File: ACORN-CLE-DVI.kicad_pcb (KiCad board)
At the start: 4 copper layers, 2 parts, among them J1 HDMI_A, U1 PI3HDX511D

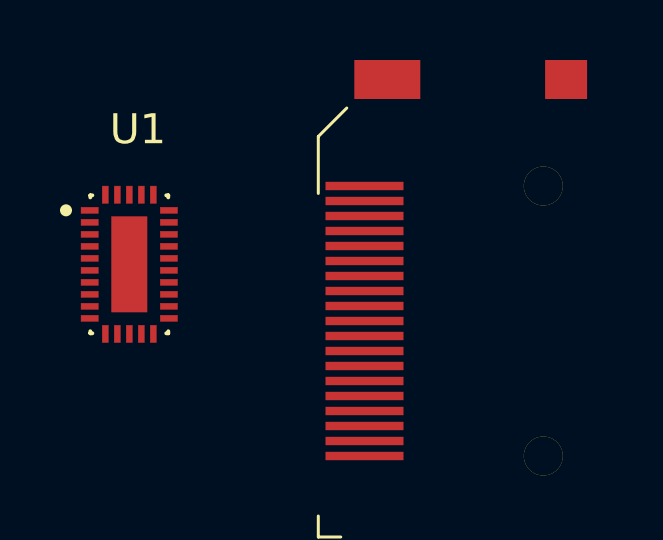
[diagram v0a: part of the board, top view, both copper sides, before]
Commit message: routed differential pairs
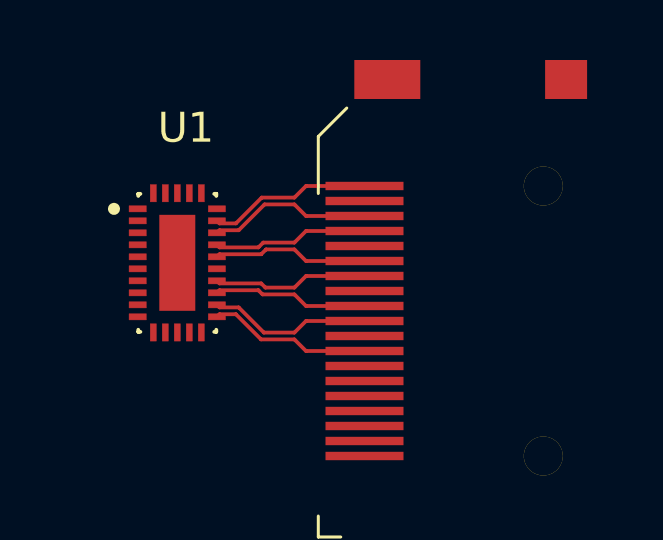
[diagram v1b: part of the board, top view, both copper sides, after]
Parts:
- moved U1 1.60 mm to (156.1, 93.0)
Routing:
- net /TMDS_OUT_D2-: track 0.00 -> 5.47 mm
- net /TMDS_OUT_D2+: track 0.00 -> 5.47 mm
- net /TMDS_OUT_CK-: track 0.00 -> 5.46 mm
- net /TMDS_OUT_CK+: track 0.00 -> 5.46 mm
- net /TMDS_OUT_D1-: track 0.00 -> 5.18 mm
- net /TMDS_OUT_D1+: track 0.00 -> 5.18 mm
- net /TMDS_OUT_D0-: track 0.00 -> 5.17 mm
- net /TMDS_OUT_D0+: track 0.00 -> 5.17 mm

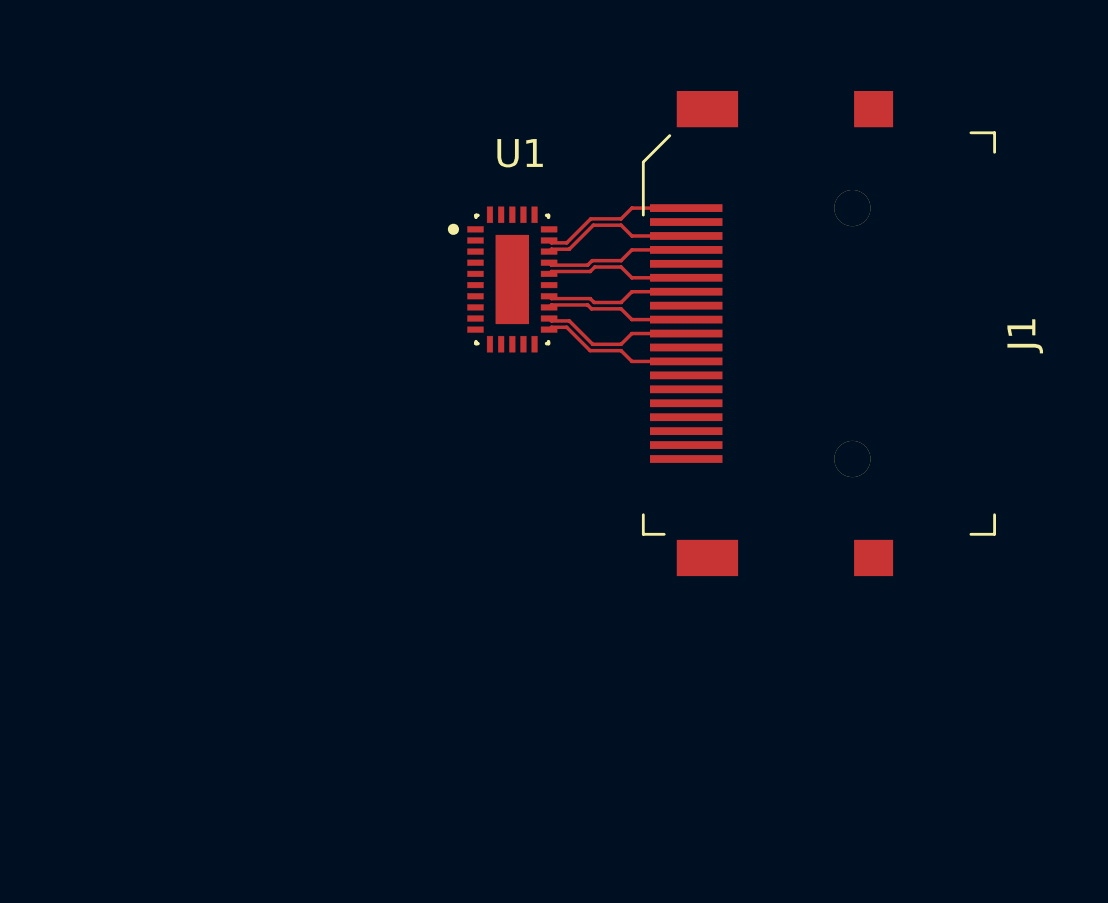
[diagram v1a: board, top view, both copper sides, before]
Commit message: schematic done, most of board routing
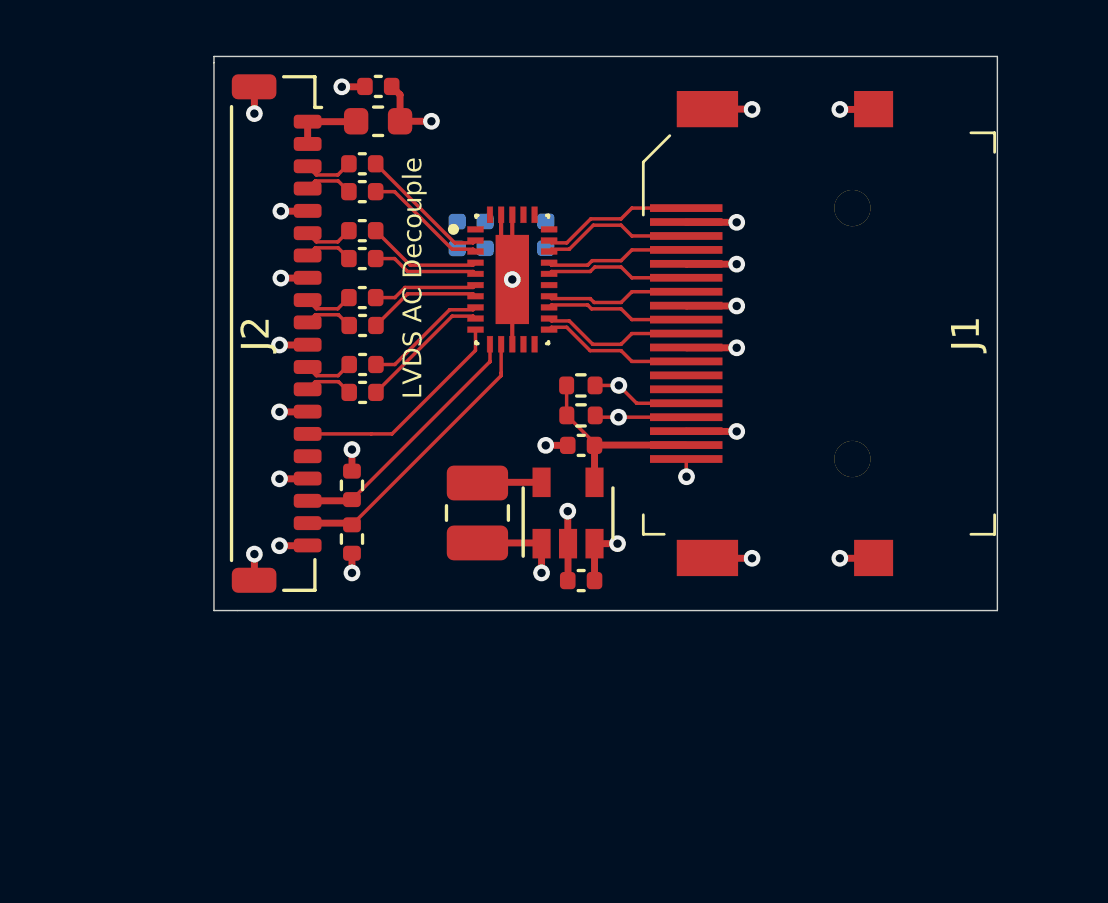
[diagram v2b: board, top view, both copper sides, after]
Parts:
- added C1: 100n, Capacitor_SMD:C_0402_1005Metric, F.Cu at (150.7, 88.9)
- added C10: 10u, Capacitor_SMD:C_0402_1005Metric, F.Cu at (151.3, 86.1)
- added C11: 100n, Capacitor_SMD:C_0402_1005Metric, B.Cu at (155.1, 91.5)
- added C12: 100n, Capacitor_SMD:C_0402_1005Metric, B.Cu at (157.3, 91.4)
- added C13: 10u, Capacitor_SMD:C_0402_1005Metric, F.Cu at (158.6, 103.8)
- added C14: 10u, Capacitor_SMD:C_0402_1005Metric, F.Cu at (158.6, 99.0)
- added C2: 100n, Capacitor_SMD:C_0402_1005Metric, F.Cu at (150.7, 89.9)
- added C3: 100n, Capacitor_SMD:C_0402_1005Metric, F.Cu at (150.7, 91.3)
- added C4: 100n, Capacitor_SMD:C_0402_1005Metric, F.Cu at (150.7, 92.3)
- added C5: 100n, Capacitor_SMD:C_0402_1005Metric, F.Cu at (150.7, 93.7)
- added C6: 100n, Capacitor_SMD:C_0402_1005Metric, F.Cu at (150.7, 94.7)
- added C7: 100n, Capacitor_SMD:C_0402_1005Metric, F.Cu at (150.7, 96.1)
- added C8: 100n, Capacitor_SMD:C_0402_1005Metric, F.Cu at (150.7, 97.1)
- added C9: 4u7, Capacitor_SMD:C_0402_1005Metric, B.Cu at (154.1, 91.5)
- added FB1: Ferrite_Bead_Small, Inductor_SMD:L_0603_1608Metric, F.Cu at (151.3, 87.4)
- added J2: Acorn, ACORN-CLE-HDMI:Hirose_DF52-20S-0.8H_1x20-1MP_P0.80mm_Horizontal, F.Cu at (147.7, 95.0)
- added L1: 4u7, Inductor_SMD:L_1008_2520Metric, F.Cu at (154.8, 101.4)
- added R1: 2K2, Resistor_SMD:R_0402_1005Metric, F.Cu at (150.3, 102.4)
- added R2: 2K2, Resistor_SMD:R_0402_1005Metric, F.Cu at (150.3, 100.4)
- added R3: 2K2, Resistor_SMD:R_0402_1005Metric, F.Cu at (158.6, 96.8)
- added R4: 2K2, Resistor_SMD:R_0402_1005Metric, F.Cu at (158.6, 97.9)
- added U2: XC9141, Package_TO_SOT_SMD:SOT-23-5, F.Cu at (158.1, 101.4)
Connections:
- U1 pad 10: Net-(U1-Pad10) -> /HPD_SOURCE
- U1 pad 11: Net-(U1-Pad11) -> /SDA_SOURCE
- U1 pad 12: Net-(U1-Pad12) -> /SCL_SOURCE
- U1 pad 2: Net-(U1-Pad2) -> /TMDS_IN_D2+
- U1 pad 29: Net-(U1-Pad29) -> GND
- U1 pad 3: Net-(U1-Pad3) -> /TMDS_IN_D2-
- U1 pad 31: Net-(U1-Pad31) -> GND
- U1 pad 4: Net-(U1-Pad4) -> /TMDS_IN_D1+
- U1 pad 5: Net-(U1-Pad5) -> /TMDS_IN_D1-
- U1 pad 6: Net-(U1-Pad6) -> /TMDS_IN_D0+
- U1 pad 7: Net-(U1-Pad7) -> /TMDS_IN_D0-
- U1 pad 8: Net-(U1-Pad8) -> /TMDS_IN_CK+
- U1 pad 9: Net-(U1-Pad9) -> /TMDS_IN_CK-
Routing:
- net GND: track 0.00 -> 33.9 mm, vias 0 -> 21
- net /SCL_SOURCE: track 0.00 -> 10.3 mm
- net +3V3: track 0.00 -> 9.49 mm, vias 0 -> 5
- net /SDA_SOURCE: track 0.00 -> 9.24 mm
- net /HPD_SOURCE: track 0.00 -> 8.01 mm
- net +5V: track 0.00 -> 7.18 mm
- net /TMDS_IN_D2+: track 0.00 -> 4.79 mm
- net /TMDS_IN_CK-: track 0.00 -> 4.74 mm
- net /TMDS_IN_D2-: track 0.00 -> 4.47 mm
- net /TMDS_IN_CK+: track 0.00 -> 4.42 mm
- net /TMDS_IN_D1+: track 0.00 -> 4.13 mm
- net /TMDS_IN_D0-: track 0.00 -> 4.08 mm
- net /TMDS_IN_D1-: track 0.00 -> 3.81 mm
- net /TMDS_IN_D0+: track 0.00 -> 3.77 mm
- net /SCL_SINK: track 0.00 -> 3.53 mm, vias 0 -> 1
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- added copper zone on In2.Cu, net +3V3
- added copper zone on In1.Cu, net GND
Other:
- board outline added: 28.1 x 19.9 mm
- board text added: "LVDS AC Decouple"

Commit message: functionally complete, need to verify before buying
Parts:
- added JP1: Equalization, Jumper:SolderJumper-3_P1.3mm_Open_RoundedPad1.0x1.5mm_NumberLabels, B.Cu at (146.2, 100.6)
- added JP2: Pre-emphasis, Jumper:SolderJumper-3_P1.3mm_Open_RoundedPad1.0x1.5mm_NumberLabels, B.Cu at (146.2, 106.3)
- moved C12 11.7 mm to (151.7, 101.7), turned to 180 degrees
- moved C13 10.2 mm to (152.9, 112.3)
- moved C14 10.2 mm to (152.9, 107.5)
- moved C3 10.2 mm to (145.1, 99.8)
- moved C4 10.2 mm to (145.1, 100.8)
- moved C5 10.2 mm to (145.1, 102.2)
- moved FB1 10.2 mm to (145.6, 95.8)
- moved L1 10.2 mm to (149.2, 109.9)
- moved R1 10.2 mm to (144.7, 110.8)
- moved R2 10.2 mm to (144.7, 108.9)
- moved R3 10.2 mm to (152.9, 105.3)
- moved R4 10.2 mm to (152.9, 106.4)
- moved U1 10.2 mm to (150.4, 101.5)
- moved U2 10.2 mm to (152.4, 109.9)
- moved C1 10.2 mm to (145.1, 97.3)
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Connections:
- U1 pad 14: Net-(U1-Pad14) -> OC
- U1 pad 15: Net-(U1-Pad15) -> EQ
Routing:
- net /HPD_SINK: track 0.64 -> 16.3 mm, vias 1 -> 2
- net GND: track 33.9 -> 48.3 mm, vias 21 -> 23
- net /SDA_SINK: track 3.29 -> 13.6 mm, vias 1 -> 2
- net /SCL_SINK: track 3.53 -> 12.9 mm, vias 1 -> 2
- net +3V3: track 9.49 -> 18.4 mm, vias 5 -> 7
- net EQ: track 0.00 -> 8.47 mm, vias 0 -> 1
- net OC: track 0.00 -> 6.45 mm, vias 0 -> 1
- net Net-(C9-Pad1): track 0.00 -> 2.26 mm, vias 0 -> 1
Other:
- board text added: "1.5dB"
- board text added: "5.0dB"
- board text added: "DVI Adapter and Redriver v1.0 Designed by Nathaniel R. Lewis <hardware@nrlewis.dev> CC-BY-SA 4.0"
- board text added: "EQ"
- board text added: "OC"
- board text removed: "LVDS AC Decouple"

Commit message: add datasheets and digikey part numbers
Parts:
- FB1: value Ferrite_Bead_Small -> 100 ohm @ 100 MHz
- renumbered C12 to C10, C10 to C11, C14 to C12, C9 to C14, C11 to C9

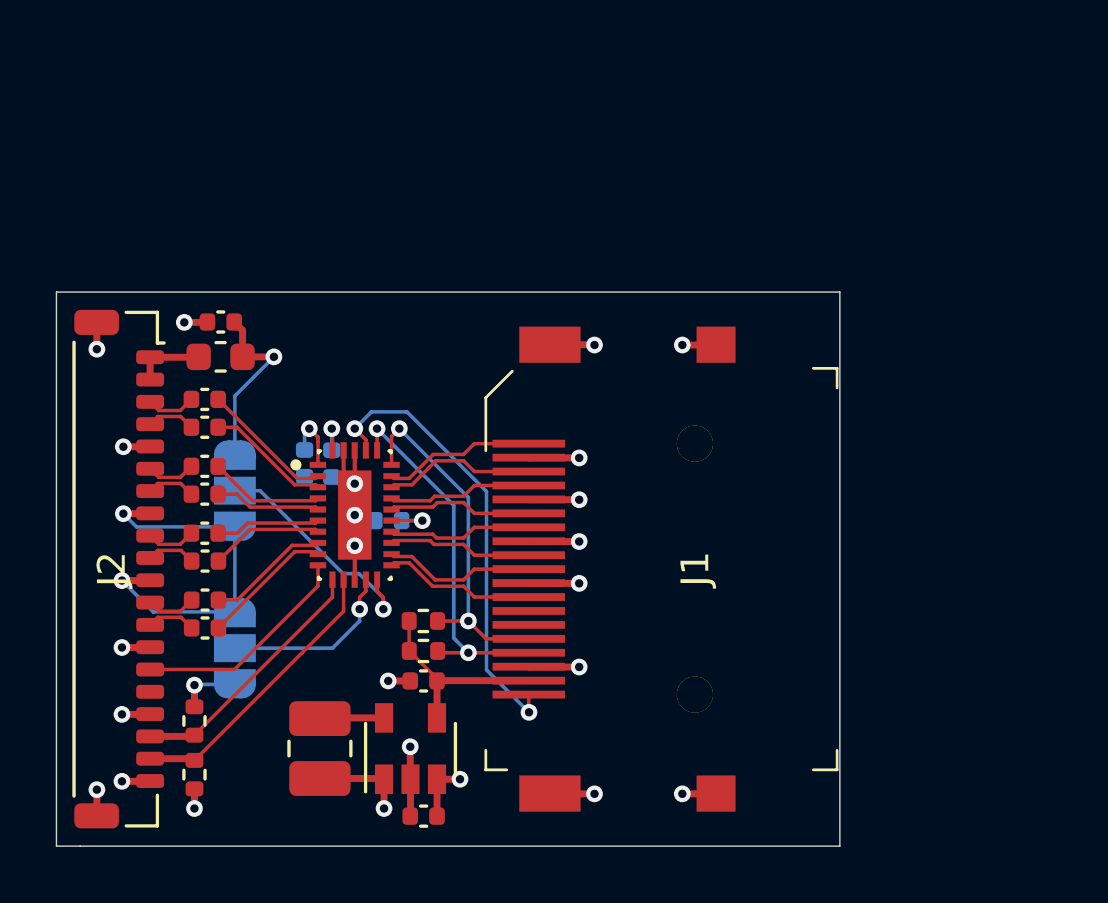
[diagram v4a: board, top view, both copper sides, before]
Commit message: correct the size of the TQFN-30 footprint
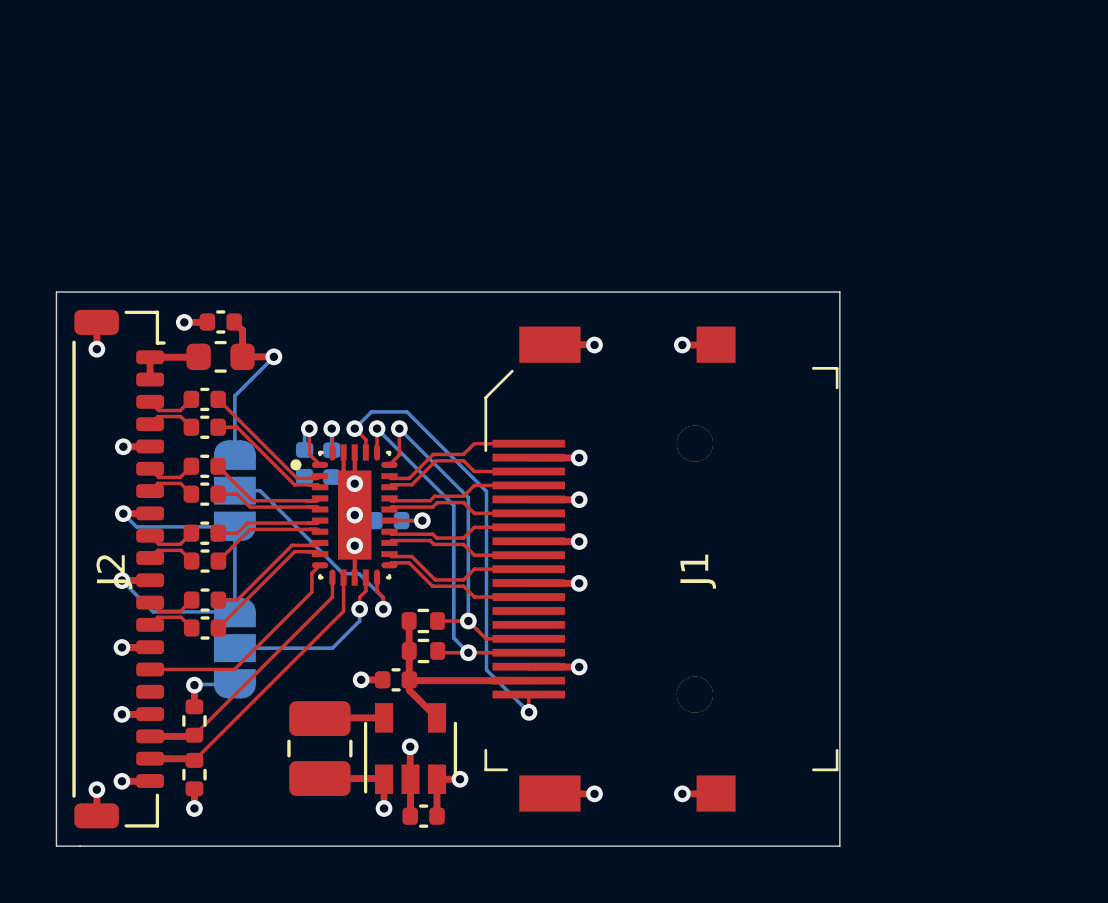
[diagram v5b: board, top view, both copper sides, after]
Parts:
- moved C12 0.99 mm to (151.9, 107.4)
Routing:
- net +5V: track 7.18 -> 8.18 mm
- net /TMDS_IN_D1+: track 4.13 -> 4.63 mm
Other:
- board text added: "DVI Adapter and Redriver v1.0 Designed by Nathan <hardware@nrlewis.dev> CC-BY-SA 4.0"
- board text removed: "DVI Adapter and Redriver v1.0 Designed by Nathaniel R. Lewis <hardware@nrlewis.dev> CC-BY-SA 4.0"

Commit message: state at manufacturing
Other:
- board text added: "DVI Adapter and Redriver v1.0"
- board text added: "Designed by Nathan <hardware@nrlewis.dev> CC-BY-SA 4.0"
- board text removed: "DVI Adapter and Redriver v1.0 Designed by Nathan <hardware@nrlewis.dev> CC-BY-SA 4.0"
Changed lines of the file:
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@@
   (general
     (thickness 1.6)
-    (drawings 29)
+    (drawings 30)
     (tracks 334)
     (zones 0)
@@
     (tags "connector Hirose  horizontal")
     (attr smd)
-    (fp_text reference J2 (at 0.001 0.26 90) (layer F.SilkS)
+    (fp_text reference J2 (at 0.001 0.26 90) (layer F.SilkS) hide
       (effects (font (size 1 1) (thickness 0.15)))
     )
@@
     (descr http://media.digikey.com/pdf/Data%20Sheets/CNC%20Tech%20PDFs/HDMI_A_Female_2000-1-2-41-00-BK_Dwg.pdf)
     (attr smd)
-    (fp_text reference J1 (at -0.009 -1.52 90) (layer F.SilkS)
+    (fp_text reference J1 (at -0.009 -1.52 90) (layer F.SilkS) hide
       (effects (font (size 1 1) (thickness 0.15)))
     )
@@
       (net 12 /TMDS_OUT_CK+))
   )
+  (gr_text "Designed by Nathan\n<hardware@nrlewis.dev>\nCC-BY-SA 4.0" (at 161.84 97.75) (layer B.SilkS)
+    (effects (font (size 0.75 0.75) (thickness 0.15)) (justify left mirror))
+  )
   (gr_text OC (at 144.43 103.72) (layer B.SilkS)
     (effects (font (size 0.85 0.85) (thickness 0.15)) (justify left mirror))
@@
     (effects (font (size 0.75 0.75) (thickness 0.15)) (justify left mirror))
   )
-  (gr_text "DVI Adapter and Redriver v1.0\n\nDesigned by Nathan\n<hardware@nrlewis.dev>\nCC-BY-SA 4.0" (at 161.86 96.84) (layer B.SilkS)
+  (gr_text "DVI Adapter and Redriver v1.0" (at 161.85 94.45) (layer B.SilkS)
     (effects (font (size 0.75 0.75) (thickness 0.15)) (justify left mirror))
   )
